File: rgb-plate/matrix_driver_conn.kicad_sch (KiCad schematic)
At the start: 10 parts, among them J1 Conn_01x27, J2 Conn_01x08, J3 Conn_01x08, J5 Conn_01x27

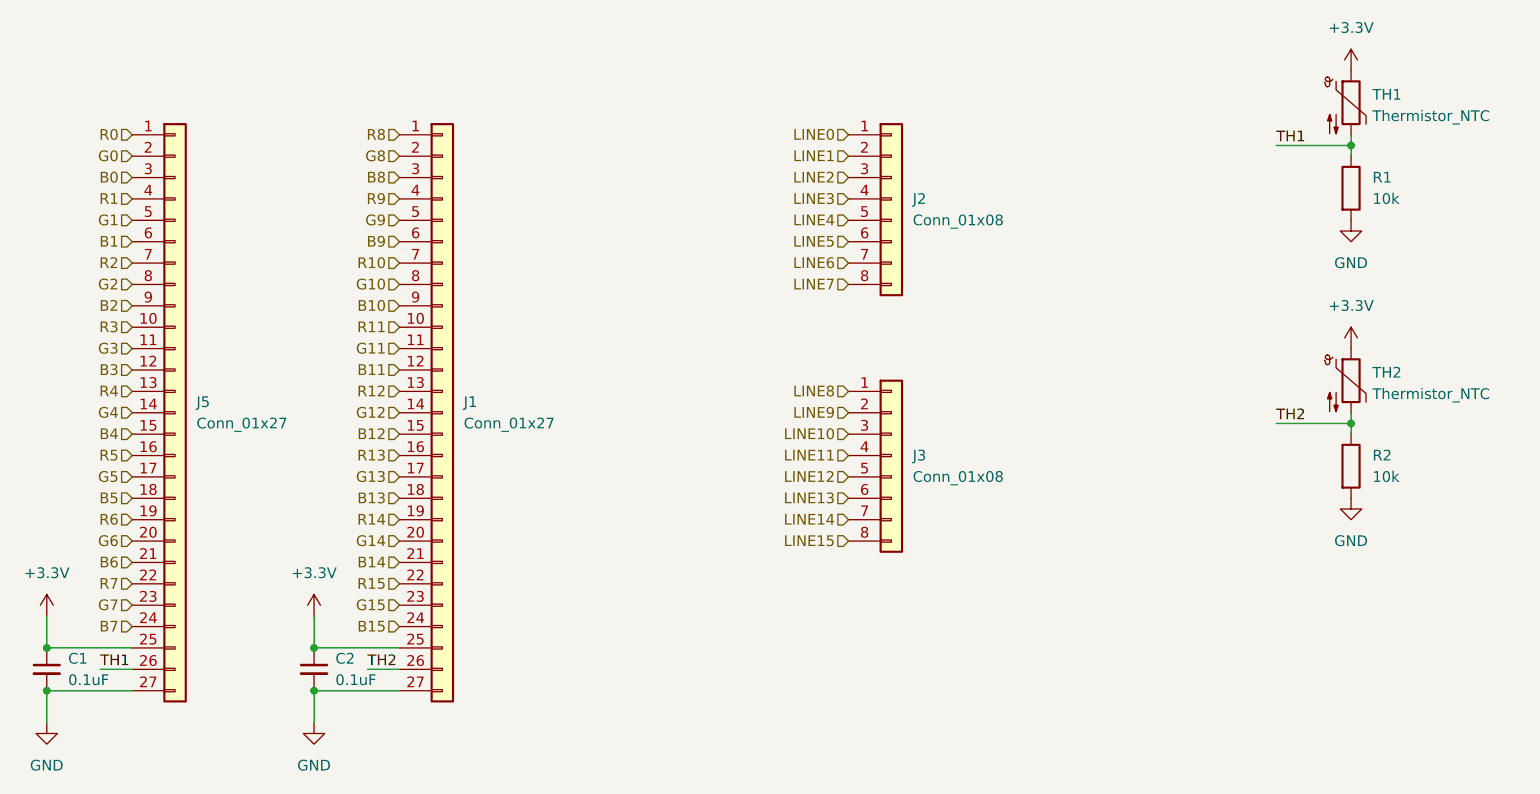
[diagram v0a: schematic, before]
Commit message: finished flipping ribbon connectors, drc pass, export gerbers, drill files, and pick and place files
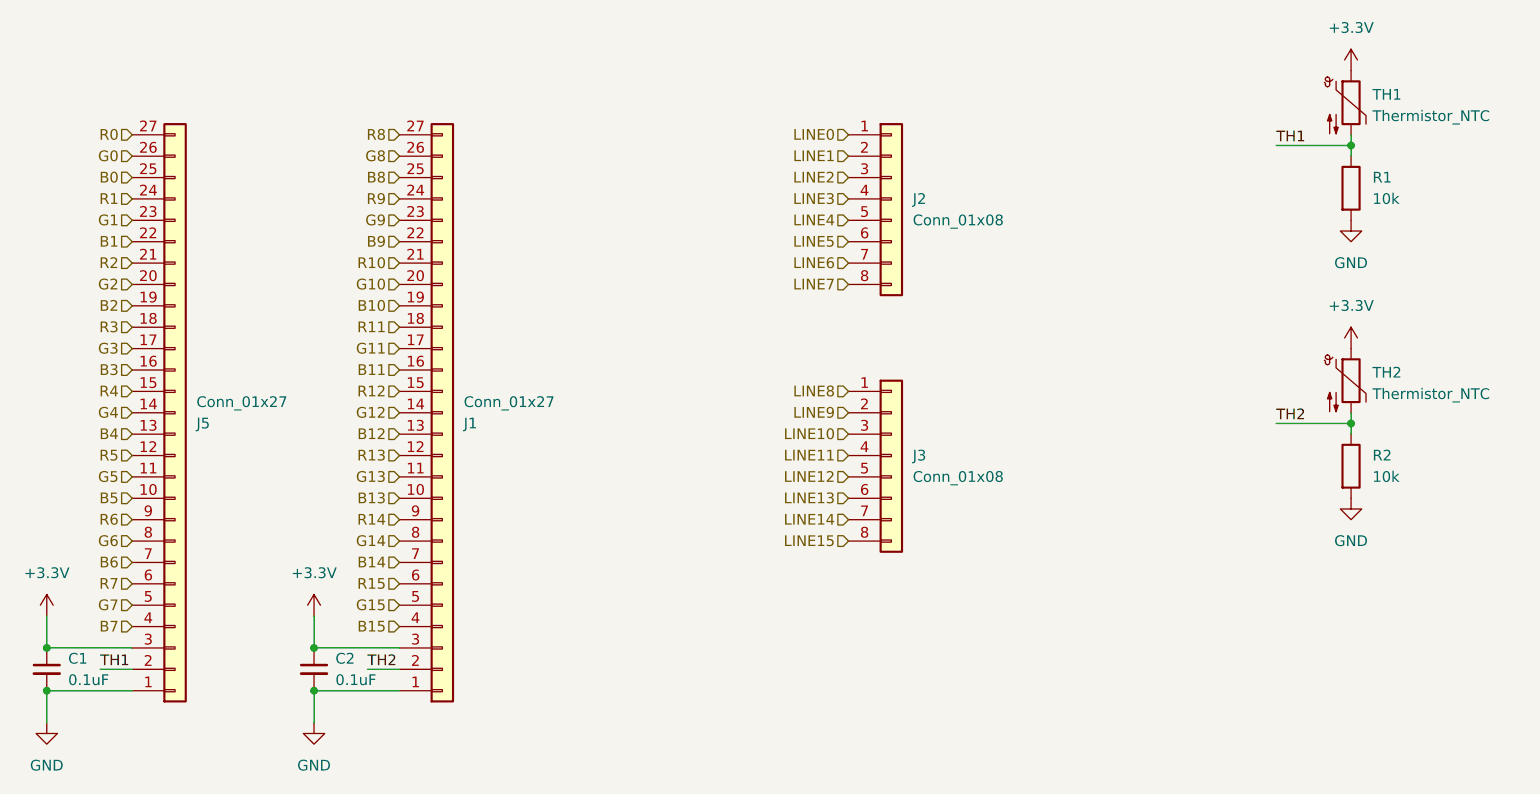
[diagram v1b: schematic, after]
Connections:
- net +3.3V: now also J1.3 (Pin_3), J5.3 (Pin_3); no longer J1.25 (Pin_25), J5.25 (Pin_25)
- net B0: now also J5.25 (Pin_25); no longer J5.3 (Pin_3)
- net B1: now also J5.22 (Pin_22); no longer J5.6 (Pin_6)
- net B10: now also J1.19 (Pin_19); no longer J1.9 (Pin_9)
- net B11: now also J1.16 (Pin_16); no longer J1.12 (Pin_12)
- net B12: now also J1.13 (Pin_13); no longer J1.15 (Pin_15)
- net B13: now also J1.10 (Pin_10); no longer J1.18 (Pin_18)
- net B14: now also J1.7 (Pin_7); no longer J1.21 (Pin_21)
- net B15: now also J1.4 (Pin_4); no longer J1.24 (Pin_24)
- net B2: now also J5.19 (Pin_19); no longer J5.9 (Pin_9)
- net B3: now also J5.16 (Pin_16); no longer J5.12 (Pin_12)
- net B4: now also J5.13 (Pin_13); no longer J5.15 (Pin_15)
- net B5: now also J5.10 (Pin_10); no longer J5.18 (Pin_18)
- net B6: now also J5.7 (Pin_7); no longer J5.21 (Pin_21)
- net B7: now also J5.4 (Pin_4); no longer J5.24 (Pin_24)
- net B8: now also J1.25 (Pin_25); no longer J1.3 (Pin_3)
- net B9: now also J1.22 (Pin_22); no longer J1.6 (Pin_6)
- net G0: now also J5.26 (Pin_26); no longer J5.2 (Pin_2)
- net G1: now also J5.23 (Pin_23); no longer J5.5 (Pin_5)
- net G10: now also J1.20 (Pin_20); no longer J1.8 (Pin_8)
- net G11: now also J1.17 (Pin_17); no longer J1.11 (Pin_11)
- net G13: now also J1.11 (Pin_11); no longer J1.17 (Pin_17)
- net G14: now also J1.8 (Pin_8); no longer J1.20 (Pin_20)
- net G15: now also J1.5 (Pin_5); no longer J1.23 (Pin_23)
- net G2: now also J5.20 (Pin_20); no longer J5.8 (Pin_8)
- net G3: now also J5.17 (Pin_17); no longer J5.11 (Pin_11)
- net G5: now also J5.11 (Pin_11); no longer J5.17 (Pin_17)
- net G6: now also J5.8 (Pin_8); no longer J5.20 (Pin_20)
- net G7: now also J5.5 (Pin_5); no longer J5.23 (Pin_23)
- net G8: now also J1.26 (Pin_26); no longer J1.2 (Pin_2)
- net G9: now also J1.23 (Pin_23); no longer J1.5 (Pin_5)
- net GND: now also J1.1 (Pin_1), J5.1 (Pin_1); no longer J1.27 (Pin_27), J5.27 (Pin_27)
- net R0: now also J5.27 (Pin_27); no longer J5.1 (Pin_1)
- net R1: now also J5.24 (Pin_24); no longer J5.4 (Pin_4)
- net R10: now also J1.21 (Pin_21); no longer J1.7 (Pin_7)
- net R11: now also J1.18 (Pin_18); no longer J1.10 (Pin_10)
- net R12: now also J1.15 (Pin_15); no longer J1.13 (Pin_13)
- net R13: now also J1.12 (Pin_12); no longer J1.16 (Pin_16)
- net R14: now also J1.9 (Pin_9); no longer J1.19 (Pin_19)
- net R15: now also J1.6 (Pin_6); no longer J1.22 (Pin_22)
- net R2: now also J5.21 (Pin_21); no longer J5.7 (Pin_7)
- net R3: now also J5.18 (Pin_18); no longer J5.10 (Pin_10)
- net R4: now also J5.15 (Pin_15); no longer J5.13 (Pin_13)
- net R5: now also J5.12 (Pin_12); no longer J5.16 (Pin_16)
- net R6: now also J5.9 (Pin_9); no longer J5.19 (Pin_19)
- net R7: now also J5.6 (Pin_6); no longer J5.22 (Pin_22)
- net R8: now also J1.27 (Pin_27); no longer J1.1 (Pin_1)
- net R9: now also J1.24 (Pin_24); no longer J1.4 (Pin_4)
- net TH1: now also J5.2 (Pin_2); no longer J5.26 (Pin_26)
- net TH2: now also J1.2 (Pin_2); no longer J1.26 (Pin_26)
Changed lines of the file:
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@@
 		(lib_id "Connector_Generic:Conn_01x27")
 		(at 123.19 105.41 0)
-		(unit 1)
-		(exclude_from_sim no)
-		(in_bom yes)
-		(on_board yes)
-		(dnp no)
-		(fields_autoplaced yes)
+		(mirror x)
+		(unit 1)
+		(exclude_from_sim no)
+		(in_bom yes)
+		(on_board yes)
+		(dnp no)
 		(property "Reference" "J1"
-			(at 125.73 104.1399 0)
+			(at 125.73 106.6801 0)
 			(effects
 				(font
@@
 		)
 		(property "Value" "Conn_01x27"
-			(at 125.73 106.6799 0)
+			(at 125.73 104.1401 0)
 			(effects
 				(font
@@
 		(lib_id "Connector_Generic:Conn_01x27")
 		(at 91.44 105.41 0)
-		(unit 1)
-		(exclude_from_sim no)
-		(in_bom yes)
-		(on_board yes)
-		(dnp no)
-		(fields_autoplaced yes)
+		(mirror x)
+		(unit 1)
+		(exclude_from_sim no)
+		(in_bom yes)
+		(on_board yes)
+		(dnp no)
 		(property "Reference" "J5"
-			(at 93.98 104.1399 0)
+			(at 93.98 106.6801 0)
 			(effects
 				(font
@@
 		)
 		(property "Value" "Conn_01x27"
-			(at 93.98 106.6799 0)
-			(effects
-				(font
+			(at 93.98 104.1401 0)
+			(effects
+				(font
